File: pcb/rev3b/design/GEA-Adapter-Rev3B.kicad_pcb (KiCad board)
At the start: 4 copper layers, 99 x 40 mm, 99 parts, among them J1 8P8C, J2 RECOVERY, Q3 CJ3407, Q4 CJ3407, Q5 MMBT3904, U10 TPS22810DBVR, U2 XIAO ESP32-C3 v1.3 (22-pad), U4 74LVC2G07, U5 74LVC2G07_3v3, U8 AP63205WU, U9 TPS22810DBVR

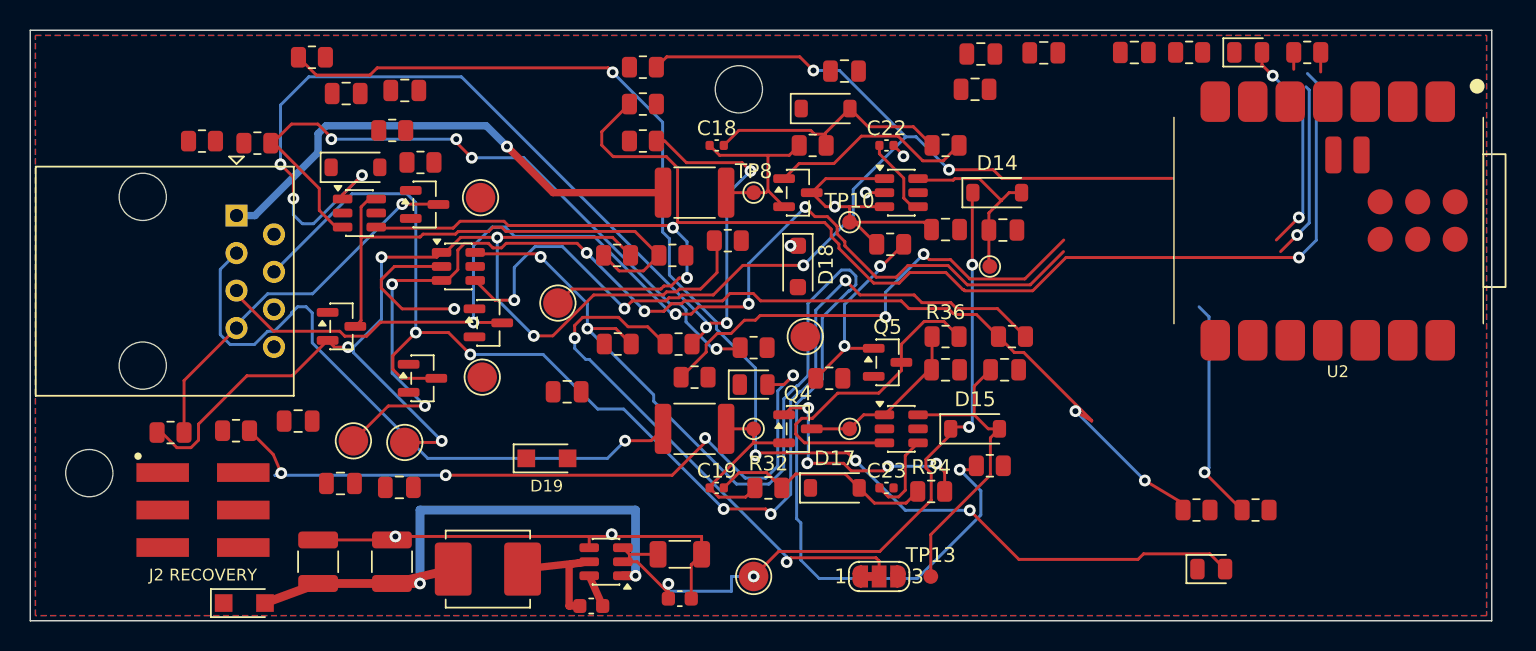
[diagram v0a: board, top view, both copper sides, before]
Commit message: feat(pcb): route Rev3B carrier connections
Preserve existing power routing and the inner ground reference. This development checkpoint still has 26 open connections and 35 power-clearance findings; it is not a fabrication release.
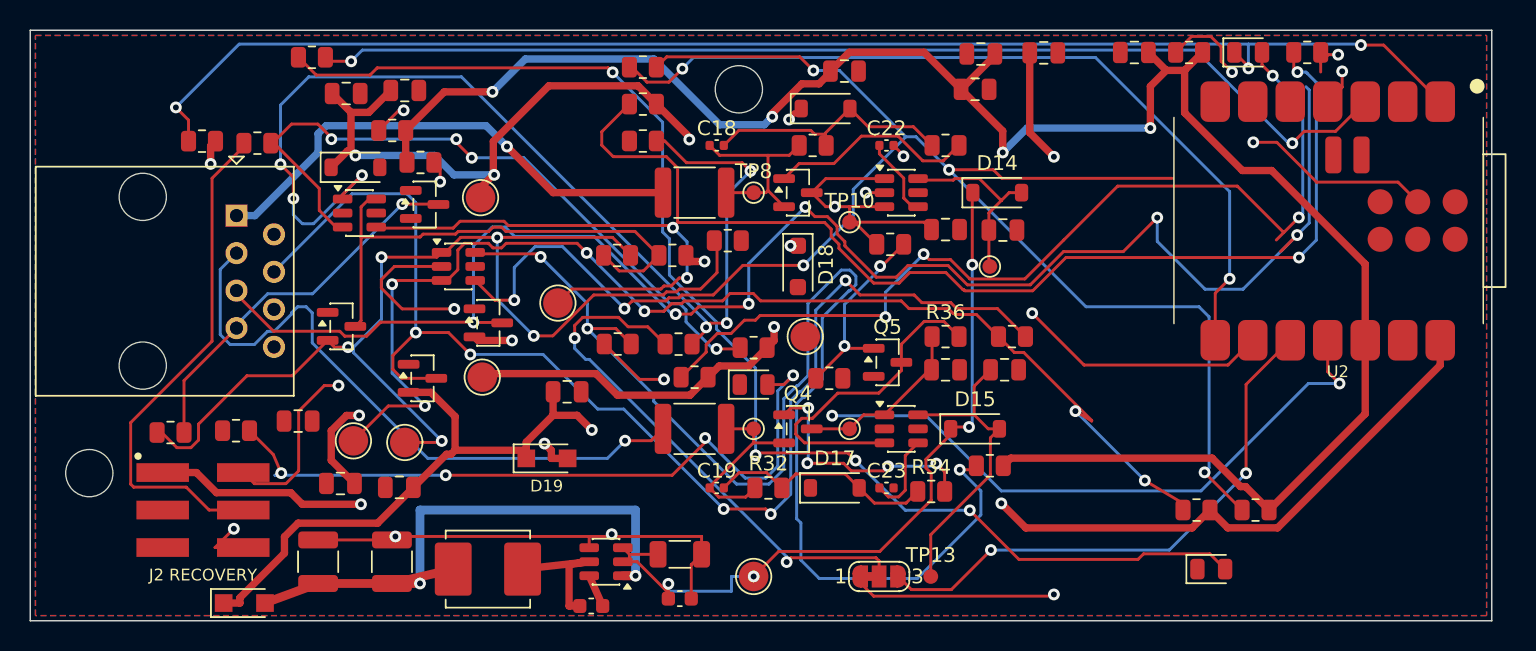
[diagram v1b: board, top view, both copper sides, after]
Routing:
- net +3V3: track 0.00 -> 227.5 mm, vias 0 -> 7
- net +5V: track 0.00 -> 213.9 mm, vias 0 -> 8
- net GEA3_TX: track 0.00 -> 104.6 mm, vias 0 -> 3
- net /DBG_LED: track 0.00 -> 94.8 mm, vias 0 -> 3
- net /LED1: track 0.00 -> 74.6 mm, vias 0 -> 2
- net /BOOT_SEL: track 0.00 -> 70.8 mm, vias 0 -> 2
- net BOOT: track 0.00 -> 67.5 mm, vias 0 -> 4
- net GEA2_RX: track 0.00 -> 60.3 mm, vias 0 -> 3
- net /GEA2_MCU_TX: track 0.00 -> 60.0 mm, vias 0 -> 2
- net GEA_FullRx: track 90.2 -> 126.2 mm, vias 5 -> 7
- net GEA3_RX: track 0.00 -> 34.6 mm
- net /5V_IN: track 0.00 -> 30.8 mm, vias 0 -> 2
- net EN: track 0.00 -> 24.0 mm, vias 0 -> 2
- net Net-(R13-Pad2): track 94.0 -> 114.8 mm
- net Net-(D5-A): track 47.1 -> 64.9 mm
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
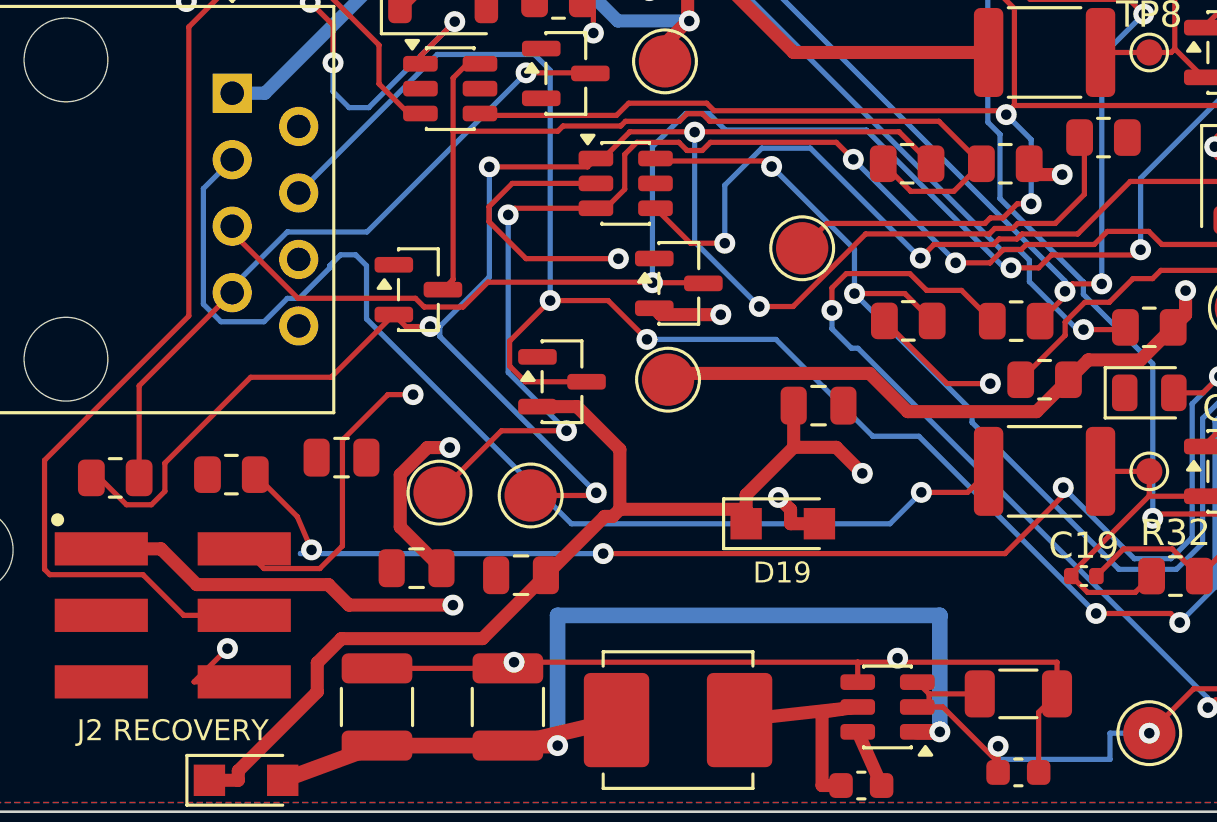
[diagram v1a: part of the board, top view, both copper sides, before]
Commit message: fix(pcb): clear Rev3B connector and input capacitor spacing
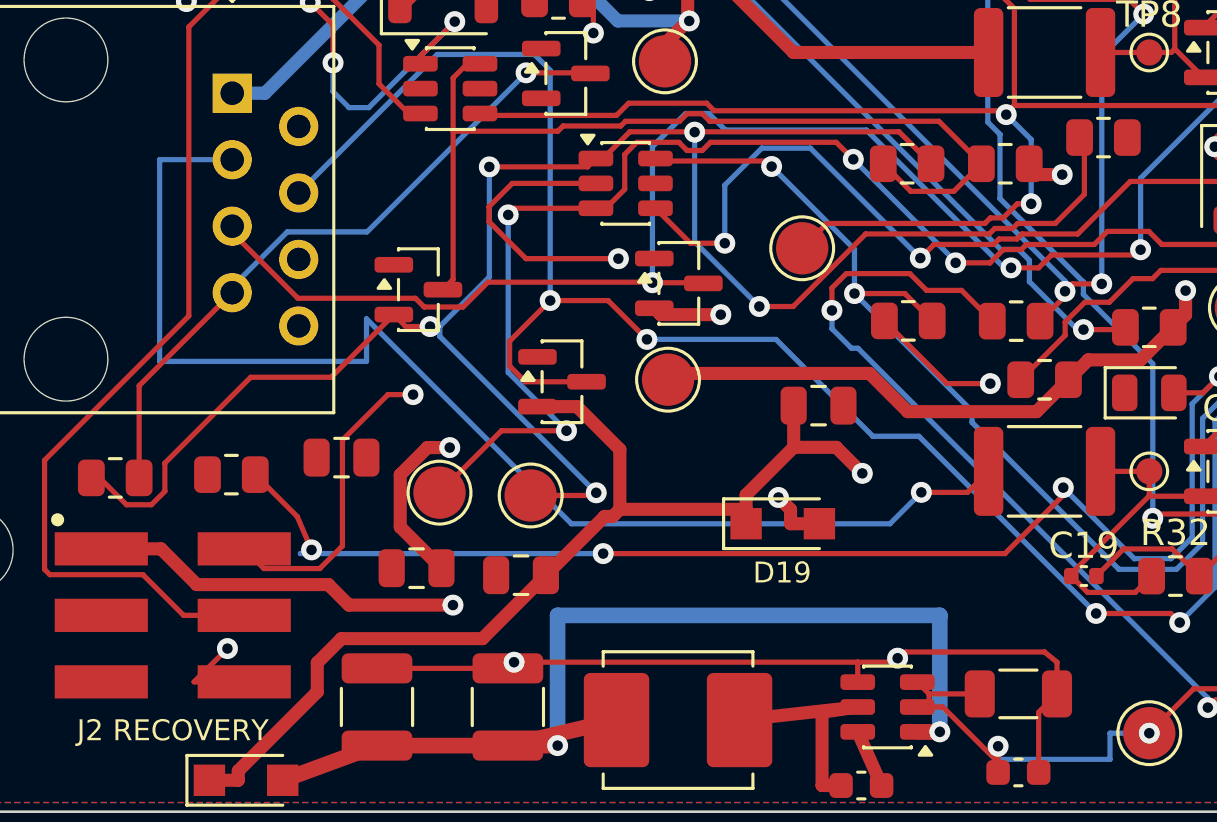
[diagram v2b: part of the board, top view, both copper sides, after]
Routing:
- net /ALT_PWR: track 43.6 -> 47.8 mm
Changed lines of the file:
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@@
 	)
 	(segment
-		(start 39.3867 34.2893)
-		(end 45.475 34.2893)
-		(width 0.2)
-		(layer "F.Cu")
-		(net 14)
-	)
-	(segment
 		(start 59.1483 8.4683)
 		(end 59.1483 8.5353)
@@
 	)
 	(segment
+		(start 39.7 33.9)
+		(end 45 33.9)
+		(width 0.2)
+		(layer "F.Cu")
+		(net 14)
+	)
+	(segment
 		(start 24.6683 16)
 		(end 23.7789 16.8894)
@@
 	)
 	(segment
+		(start 39.3867 34.2893)
+		(end 39.7 33.9)
+		(width 0.2)
+		(layer "F.Cu")
+		(net 14)
+	)
+	(segment
 		(start 27.8625 16)
 		(end 24.6683 16)
@@
 	)
 	(segment
+		(start 45 33.9)
+		(end 45.475 34.2893)
+		(width 0.2)
+		(layer "F.Cu")
+		(net 14)
+	)
+	(segment
 		(start 39.3867 34.2893)
 		(end 37.8625 34.2893)
@@
 	)
 	(segment
-		(start 19.1004 19.1416)
-		(end 18.6893 18.7305)
-		(width 0.2)
-		(layer "B.Cu")
-		(net 46)
-	)
-	(segment
-		(start 16.0744 20.3933)
-		(end 15.184 21.2837)
-		(width 0.2)
-		(layer "B.Cu")
-		(net 46)
-	)
-	(segment
-		(start 12.8687 16.1963)
-		(end 13.97 15.095)
+		(start 11.2 22.8)
+		(end 19.1004 22.8)
 		(width 0.2)
 		(layer "B.Cu")
@@
 	)
 	(segment
-		(start 17.697 19.1417)
-		(end 17.697 19.2238)
-		(width 0.2)
-		(layer "B.Cu")
-		(net 46)
-	)
-	(segment
-		(start 18.6893 18.7305)
-		(end 18.1082 18.7305)
-		(width 0.2)
-		(layer "B.Cu")
-		(net 46)
-	)
-	(segment
 		(start 39.0929 29.0022)
 		(end 26.9275 29.0022)
@@
 	)
 	(segment
-		(start 15.184 21.2837)
-		(end 13.5385 21.2837)
+		(start 13.97 15.095)
+		(end 11.2 15.095)
 		(width 0.2)
 		(layer "B.Cu")
@@
 	)
 	(segment
-		(start 19.1004 21.1751)
-		(end 19.1004 19.1416)
+		(start 11.2 15.095)
+		(end 11.2 22.8)
 		(width 0.2)
 		(layer "B.Cu")
@@
 	)
 	(segment
-		(start 17.697 19.2238)
-		(end 16.5275 20.3933)
+		(start 19.1004 22.8)
+		(end 19.1004 21.1751)
 		(width 0.2)
 		(layer "B.Cu")
@@
 		(width 0.2)
 		(layer "B.Cu")
-		(net 46)
-	)
-	(segment
-		(start 12.8687 20.6139)
-		(end 12.8687 16.1963)
-		(width 0.2)
-		(layer "B.Cu")
-		(net 46)
-	)
-	(segment
-		(start 18.1082 18.7305)
-		(end 17.697 19.1417)
-		(width 0.2)
-		(layer "B.Cu")
-		(net 46)
-	)
-	(segment
-		(start 13.5385 21.2837)
-		(end 12.8687 20.6139)
-		(width 0.2)
-		(layer "B.Cu")
-		(net 46)
-	)
-	(segment
-		(start 16.5275 20.3933)
-		(end 16.0744 20.3933)
-		(width 0.2)
-		(layer "B.Cu")

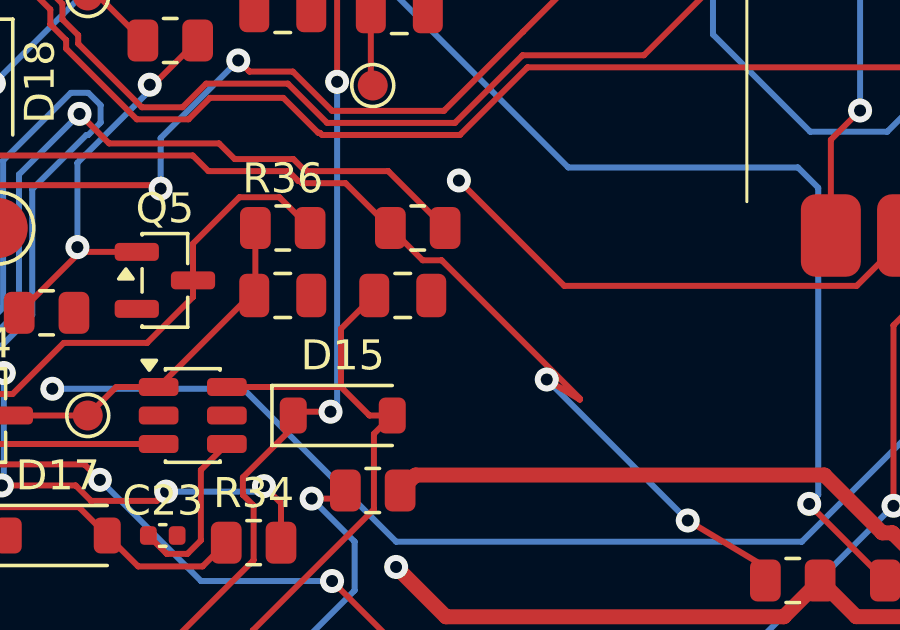
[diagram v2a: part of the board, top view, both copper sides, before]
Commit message: fix(pcb): connect Rev3B switch capacitor ground return
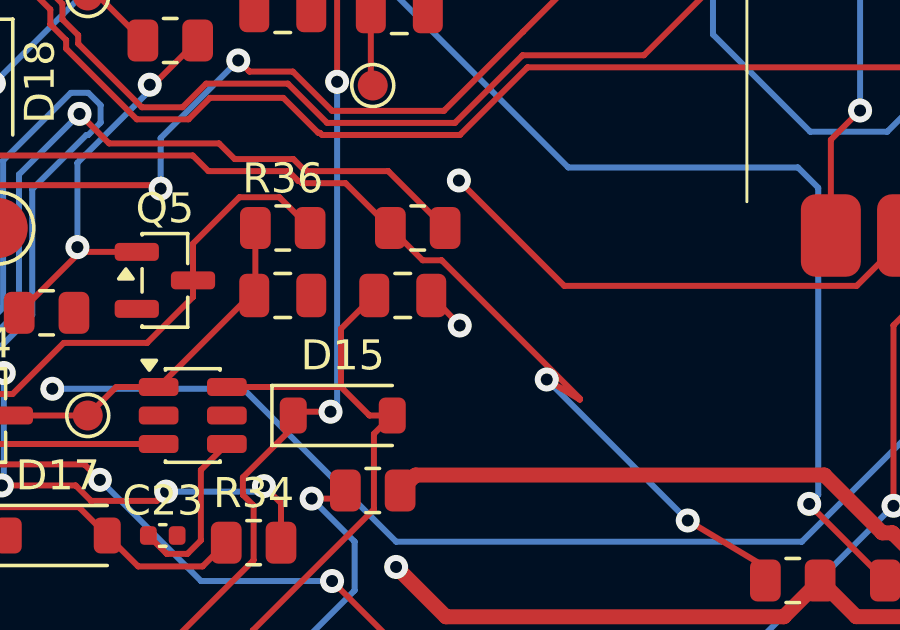
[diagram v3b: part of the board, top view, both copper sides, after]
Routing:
- net GND: track 45.2 -> 46.6 mm, vias 6 -> 7
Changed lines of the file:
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@@
+	)
+	(segment
+		(start 66.95 23)
+		(end 67.9 24)
+		(width 0.2)
+		(layer "F.Cu")
+		(net 14)
 	)
 	(segment
@@
 		(size 0.8)
 		(drill 0.4)
+		(layers "F.Cu" "B.Cu")
+		(net 14)
+	)
+	(via
+		(at 67.9 24)
+		(size 0.8)
+		(drill 0.4)

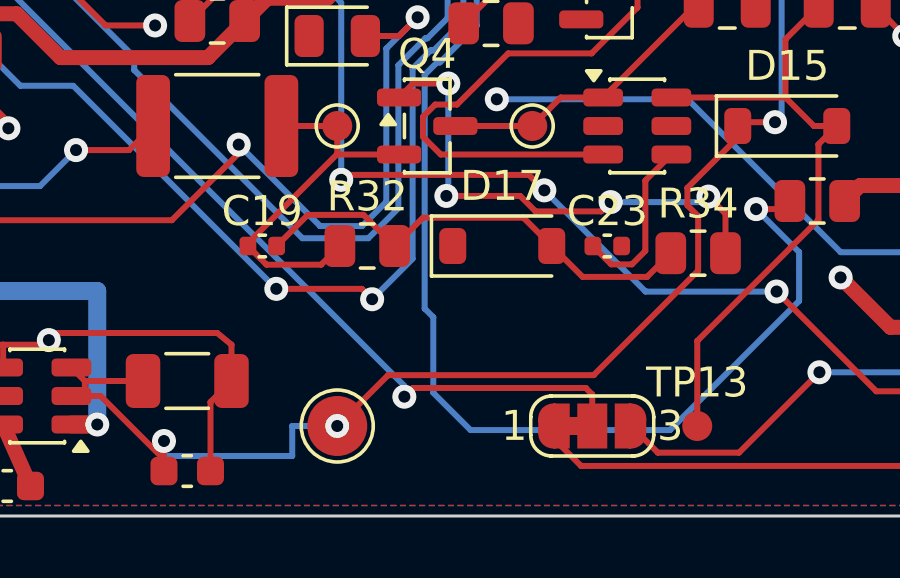
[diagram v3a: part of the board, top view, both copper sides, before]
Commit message: fix(pcb): separate Rev3B signal paths from input rails
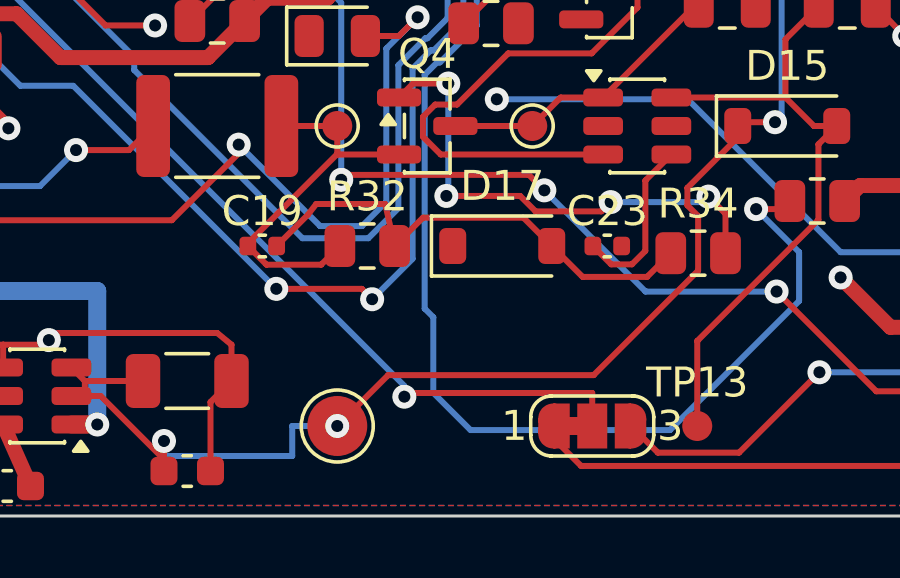
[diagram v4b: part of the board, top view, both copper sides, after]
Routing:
- net /PIN3_GATE_CLAMP: track 15.5 -> 16.4 mm
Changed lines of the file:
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@@
 	)
 	(segment
-		(start 36.8783 19.9936)
-		(end 37.4254 19.4465)
-		(width 0.2)
-		(layer "F.Cu")
-		(net 8)
-	)
-	(segment
-		(start 57.5 35.9483)
-		(end 57.2845 35.7328)
+		(start 57.5 35.9)
+		(end 57.5 37)
 		(width 0.2)
 		(layer "F.Cu")
@@
 	)
 	(segment
-		(start 57.2845 35.7328)
-		(end 51.527 35.7328)
+		(start 36.8783 19.9936)
+		(end 37.4254 19.4465)
 		(width 0.2)
 		(layer "F.Cu")
@@
 	)
 	(segment
-		(start 51.527 35.7328)
-		(end 51.2367 36.0231)
+		(start 51.2367 36.0231)
+		(end 51.5 35.9)
 		(width 0.2)
 		(layer "F.Cu")
@@
 	)
 	(segment
-		(start 41.8283 20.0867)
-		(end 43.0034 21.2618)
+		(start 51.5 35.9)
+		(end 57.5 35.9)
 		(width 0.2)
 		(layer "F.Cu")
@@
 	)
 	(segment
-		(start 57.5 37)
-		(end 57.5 35.9483)
+		(start 41.8283 20.0867)
+		(end 43.0034 21.2618)
 		(width 0.2)
 		(layer "F.Cu")
@@
 	)
 	(segment
-		(start 57.1806 32.0306)
-		(end 59.3253 32.0306)
+		(start 48.3 29.6)
+		(end 50.6 29.6)
 		(width 0.2)
 		(layer "F.Cu")
@@
 	)
 	(segment
-		(start 48.0168 29.9632)
-		(end 49.8757 29.9632)
+		(start 46.98 31)
+		(end 48.0168 29.9632)
 		(width 0.2)
 		(layer "F.Cu")
@@
 	)
 	(segment
-		(start 49.8757 29.9632)
-		(end 50.9125 31)
+		(start 57.1806 32.0306)
+		(end 59.3253 32.0306)
+		(width 0.2)
+		(layer "F.Cu")
+		(net 36)
+	)
+	(segment
+		(start 48.0168 29.9632)
+		(end 48.3 29.6)
 		(width 0.2)
 		(layer "F.Cu")
@@
 	)
 	(segment
-		(start 46.98 31)
-		(end 48.0168 29.9632)
+		(start 50.6 29.6)
+		(end 50.9125 31)
 		(width 0.2)
 		(layer "F.Cu")

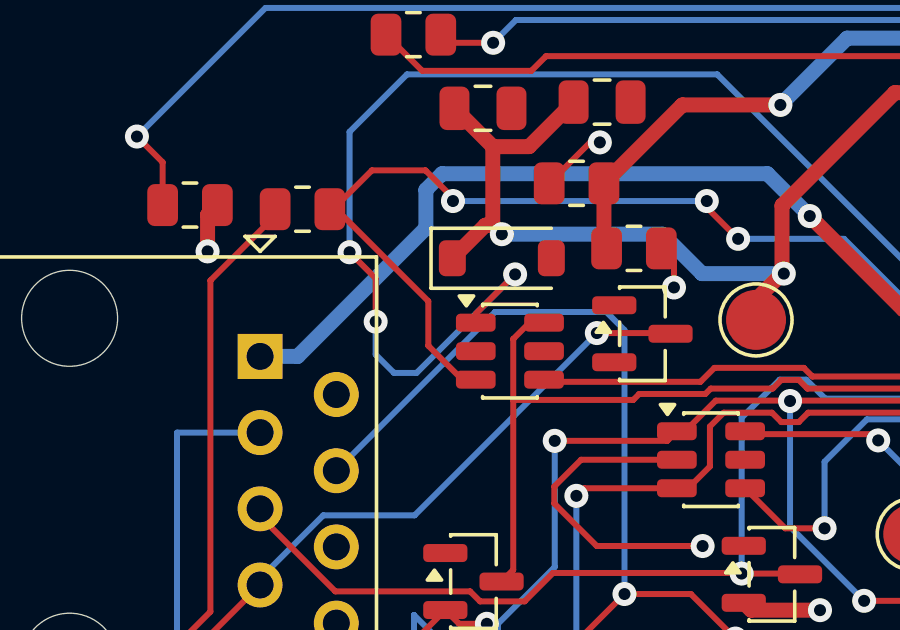
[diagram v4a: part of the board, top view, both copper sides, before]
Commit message: fix(pcb): connect Rev3B bus buffer ground return
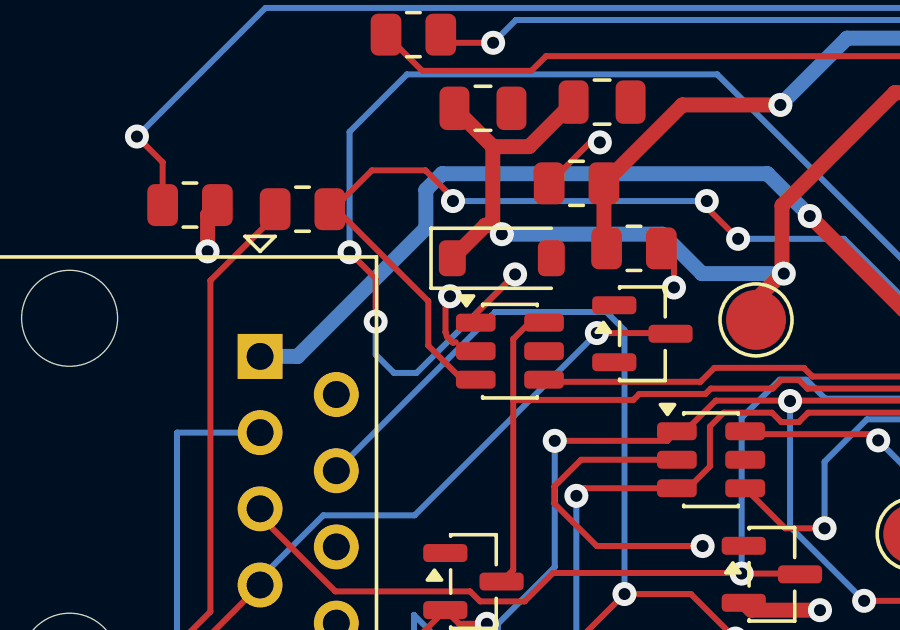
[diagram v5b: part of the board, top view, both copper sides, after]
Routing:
- net GND: track 46.6 -> 48.4 mm, vias 7 -> 8
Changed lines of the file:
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@@
+	)
+	(segment
+		(start 20.15 10.7)
+		(end 20.3 10.55)
+		(width 0.2)
+		(layer "F.Cu")
+		(net 14)
 	)
 	(segment
@@
 		(start 24.6683 16)
 		(end 23.7789 16.8894)
+		(width 0.2)
+		(layer "F.Cu")
+		(net 14)
+	)
+	(segment
+		(start 20.15 11.75)
+		(end 20.15 10.7)
 		(width 0.2)
 		(layer "F.Cu")
@@
 	)
 	(segment
+		(start 20.4 12.1)
+		(end 20.2 11.9)
+		(width 0.2)
+		(layer "F.Cu")
+		(net 14)
+	)
+	(segment
 		(start 39.3867 34.2893)
 		(end 37.8625 34.2893)
@@
 	)
 	(segment
+		(start 20.4969 12.0807)
+		(end 20.4 12.1)
+		(width 0.2)
+		(layer "F.Cu")
+		(net 14)
+	)
+	(segment
 		(start 24.7357 34.2893)
 		(end 24.5 34.525)
@@
 		(start 23.7789 16.8894)
 		(end 23.7789 17.4622)
+		(width 0.2)
+		(layer "F.Cu")
+		(net 14)
+	)
+	(segment
+		(start 20.2 11.9)
+		(end 20.15 11.75)
 		(width 0.2)
 		(layer "F.Cu")
@@
 		(size 0.8)
 		(drill 0.4)
+		(layers "F.Cu" "B.Cu")
+		(net 14)
+	)
+	(via
+		(at 20.3 10.55)
+		(size 0.8)
+		(drill 0.4)
